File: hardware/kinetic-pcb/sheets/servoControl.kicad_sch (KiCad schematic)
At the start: 2 parts

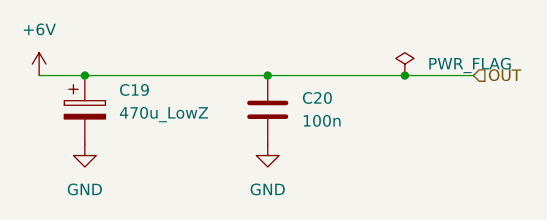
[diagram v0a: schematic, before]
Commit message: Adapt Power PCB to logic requirements
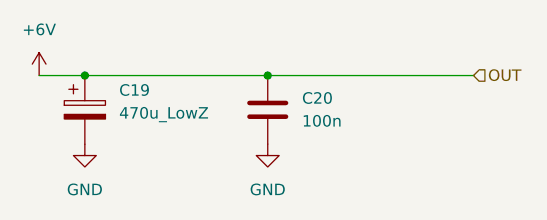
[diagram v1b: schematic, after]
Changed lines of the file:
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@@
 	(paper "A4")
-	(junction
-		(at 135.89 54.61)
-		(diameter 0)
-		(color 0 0 0 0)
-	)
 	(junction
 		(at 120.65 54.61)
@@
 	(wire
 		(pts
-			(xy 120.65 54.61) (xy 135.89 54.61)
-		)
-		(stroke
-			(width 0)
-			(type default)
-		)
-	)
-	(wire
-		(pts
-			(xy 143.51 54.61) (xy 135.89 54.61)
+			(xy 120.65 54.61) (xy 143.51 54.61)
 		)
 		(stroke
@@
 		)
 	)
-	(symbol
-		(lib_id "power:PWR_FLAG")
-		(at 135.89 54.61 0)
-		(unit 1)
-		(exclude_from_sim no)
-		(in_bom yes)
-		(on_board yes)
-		(dnp no)
-		(fields_autoplaced yes)
-		(property "Reference" "#FLG04"
-			(at 135.89 52.705 0)
-			(effects
-				(font
-					(size 1.27 1.27)
-				)
-				(hide yes)
-			)
-		)
-		(property "Value" "PWR_FLAG"
-			(at 138.43 53.3399 0)
-			(effects
-				(font
-					(size 1.27 1.27)
-				)
-				(justify left)
-			)
-		)
-		(property "Footprint" ""
-			(at 135.89 54.61 0)
-			(effects
-				(font
-					(size 1.27 1.27)
-				)
-				(hide yes)
-			)
-		)
-		(property "Datasheet" "~"
-			(at 135.89 54.61 0)
-			(effects
-				(font
-					(size 1.27 1.27)
-				)
-				(hide yes)
-			)
-		)
-		(property "Description" "Special symbol for telling ERC where power comes from"
-			(at 135.89 54.61 0)
-			(effects
-				(font
-					(size 1.27 1.27)
-				)
-				(hide yes)
-			)
-		)
-		(pin "1"
-		)
-		(instances
-			(project "logic-pcb"
-				(path "/27daf012-9196-46de-9851-628d059dd653/b945c7c4-bd95-4cd8-bb0c-9d4f2bdb338b"
-					(reference "#FLG010")
-					(unit 1)
-				)
-				(path "/27daf012-9196-46de-9851-628d059dd653/7c08b3f2-f8ea-48b3-b1b2-c164f9266479/3b6a4abe-f450-4a91-b229-31a85258e24c"
-					(reference "#FLG015")
-					(unit 1)
-				)
-				(path "/27daf012-9196-46de-9851-628d059dd653/7c08b3f2-f8ea-48b3-b1b2-c164f9266479/d76cf8f7-2816-47d3-8351-149253563630"
-					(reference "#FLG05")
-					(unit 1)
-				)
-				(path "/27daf012-9196-46de-9851-628d059dd653/bbd5f8b3-c046-4163-8596-7b069c562c38/3b6a4abe-f450-4a91-b229-31a85258e24c"
-					(reference "#FLG020")
-					(unit 1)
-				)
-				(path "/27daf012-9196-46de-9851-628d059dd653/bbd5f8b3-c046-4163-8596-7b069c562c38/d76cf8f7-2816-47d3-8351-149253563630"
-					(reference "#FLG014")
-					(unit 1)
-				)
-				(path "/27daf012-9196-46de-9851-628d059dd653/7c08b3f2-f8ea-48b3-b1b2-c164f9266479/4d5b0c5c-d13b-4b25-97fc-782a6fae8331/778d84c9-a653-4583-a8bd-59dce4292f34"
-					(reference "#FLG04")
-					(unit 1)
-				)
-				(path "/27daf012-9196-46de-9851-628d059dd653/7c08b3f2-f8ea-48b3-b1b2-c164f9266479/7f378b55-470b-4d83-93e2-fa88f5355a68/778d84c9-a653-4583-a8bd-59dce4292f34"
-					(reference "#FLG08")
-					(unit 1)
-				)
-				(path "/27daf012-9196-46de-9851-628d059dd653/7c08b3f2-f8ea-48b3-b1b2-c164f9266479/cd0cb6bb-19d2-4ea2-899a-beb1c81d5cae/778d84c9-a653-4583-a8bd-59dce4292f34"
-					(reference "#FLG012")
-					(unit 1)
-				)
-				(path "/27daf012-9196-46de-9851-628d059dd653/7c08b3f2-f8ea-48b3-b1b2-c164f9266479/d9cb5204-aa42-494f-8f48-de772f73f80a/778d84c9-a653-4583-a8bd-59dce4292f34"
-					(reference "#FLG06")
-					(unit 1)
-				)
-				(path "/27daf012-9196-46de-9851-628d059dd653/bbd5f8b3-c046-4163-8596-7b069c562c38/4d5b0c5c-d13b-4b25-97fc-782a6fae8331/778d84c9-a653-4583-a8bd-59dce4292f34"
-					(reference "#FLG07")
-					(unit 1)
-				)
-				(path "/27daf012-9196-46de-9851-628d059dd653/bbd5f8b3-c046-4163-8596-7b069c562c38/7f378b55-470b-4d83-93e2-fa88f5355a68/778d84c9-a653-4583-a8bd-59dce4292f34"
-					(reference "#FLG013")
-					(unit 1)
-				)
-				(path "/27daf012-9196-46de-9851-628d059dd653/bbd5f8b3-c046-4163-8596-7b069c562c38/cd0cb6bb-19d2-4ea2-899a-beb1c81d5cae/778d84c9-a653-4583-a8bd-59dce4292f34"
-					(reference "#FLG09")
-					(unit 1)
-				)
-				(path "/27daf012-9196-46de-9851-628d059dd653/bbd5f8b3-c046-4163-8596-7b069c562c38/d9cb5204-aa42-494f-8f48-de772f73f80a/778d84c9-a653-4583-a8bd-59dce4292f34"
-					(reference "#FLG011")
-					(unit 1)
-				)
-			)
-		)
-	)
